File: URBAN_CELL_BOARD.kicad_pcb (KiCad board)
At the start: 2 copper layers, 162 x 181.6 mm, 18 parts, among them J1 Conn_02x09_Odd_Even, J2 Conn_01x02_Female, J3 Conn_01x02_Female

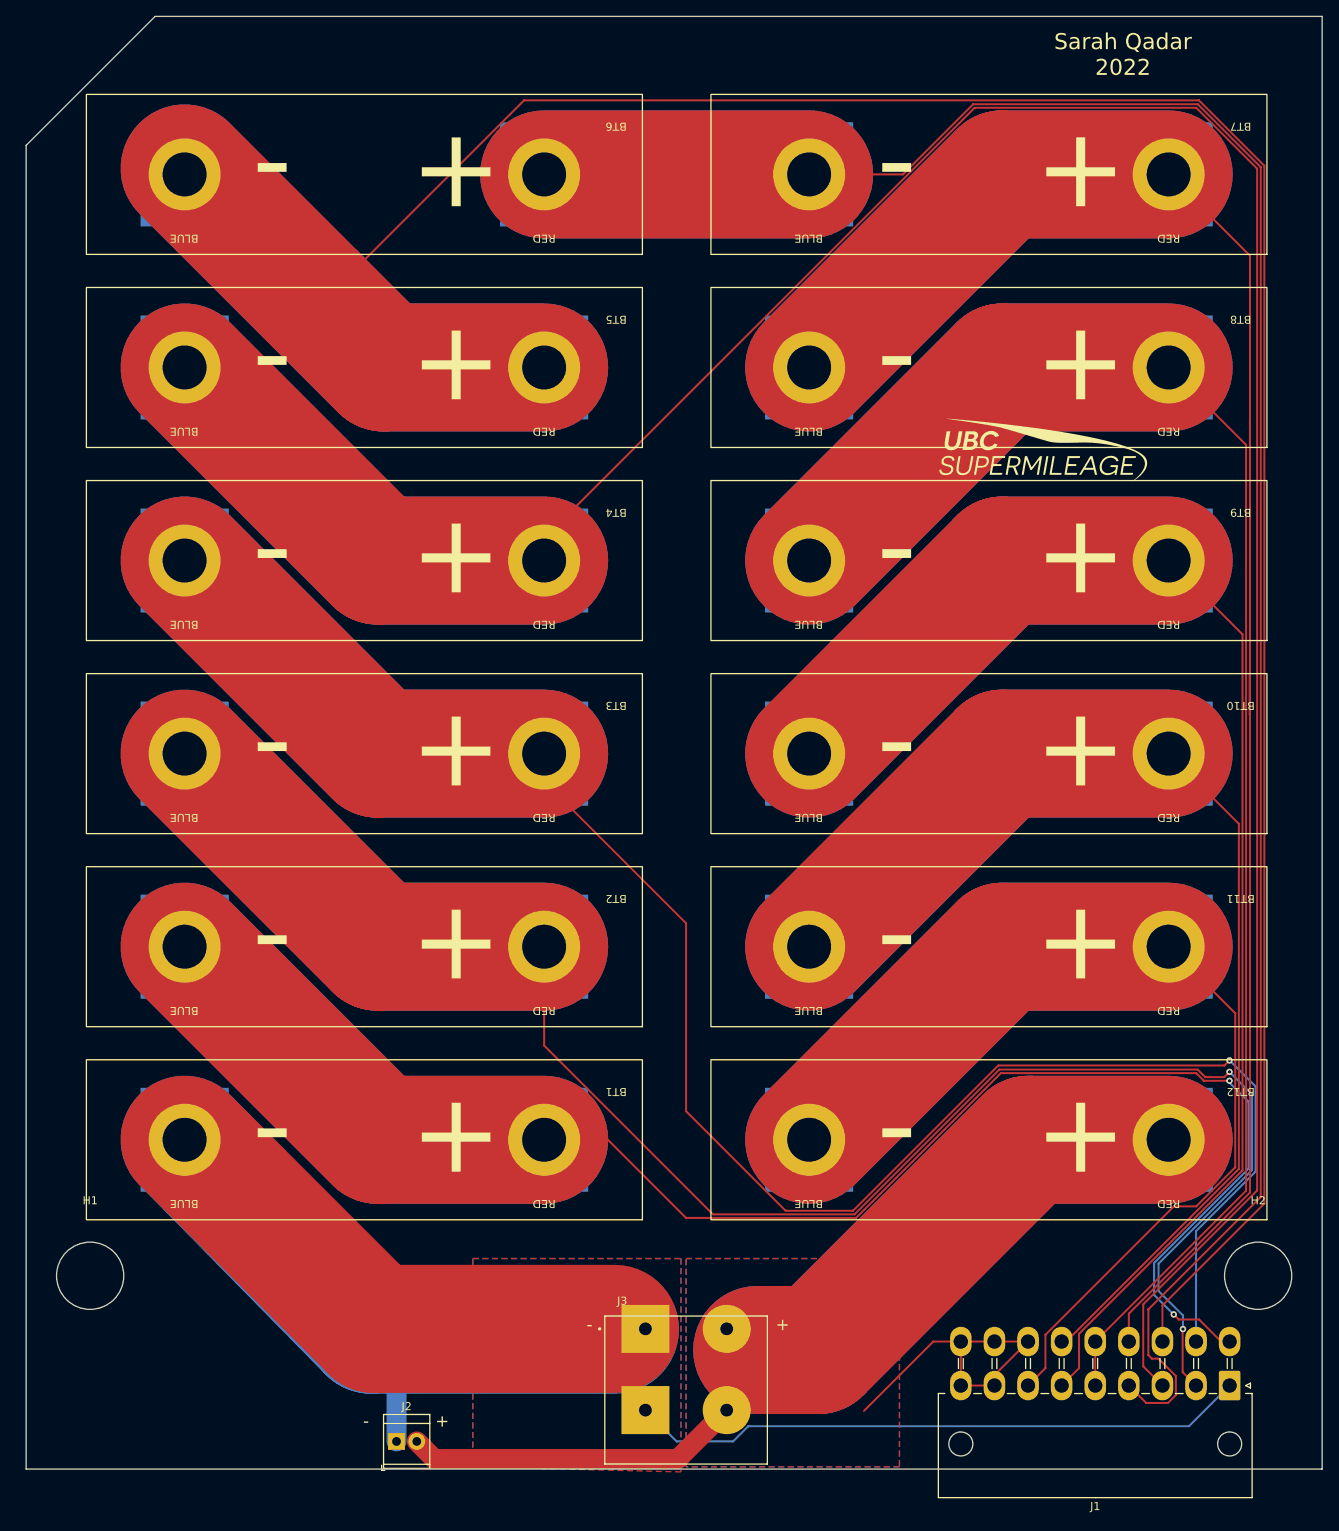
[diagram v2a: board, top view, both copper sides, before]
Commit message: fixed most layout errors/warnings
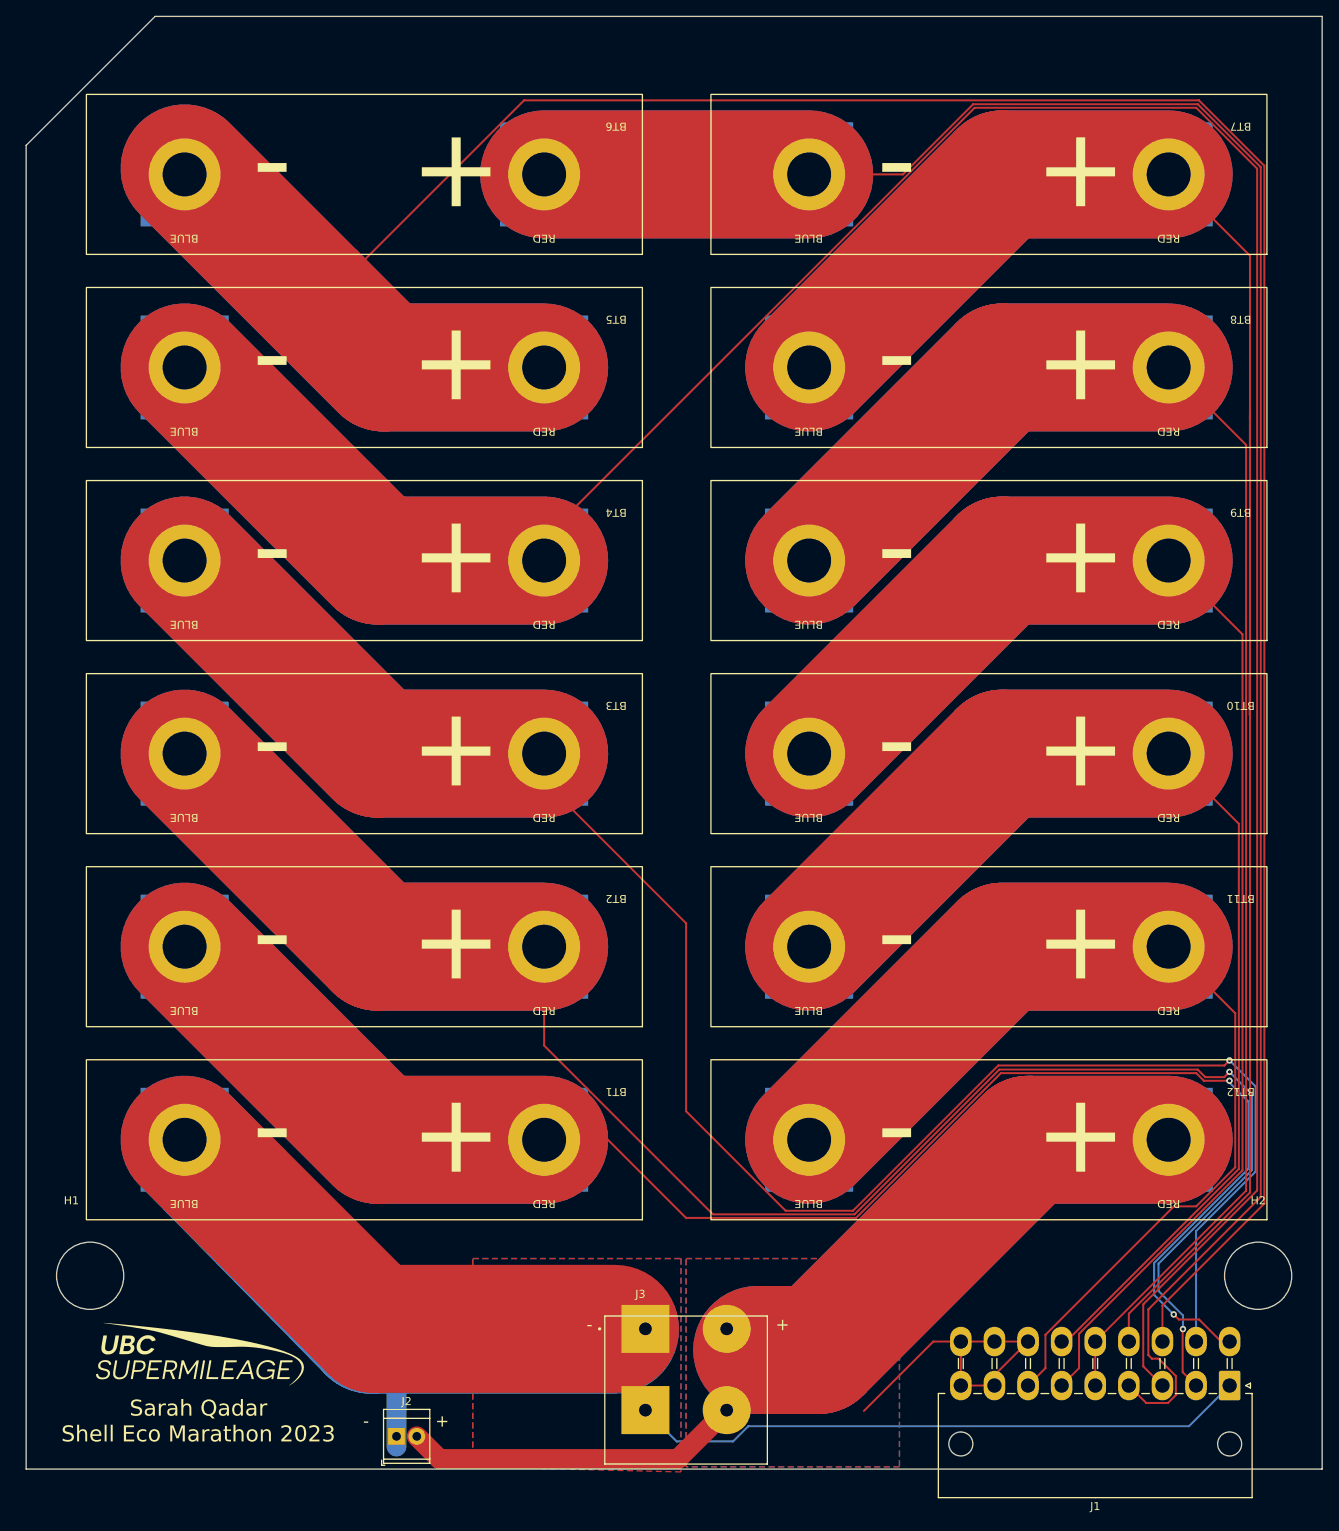
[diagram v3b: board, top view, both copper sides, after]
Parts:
- moved G*** 154.6 mm to (105.4, 268.0)
- moved J2 0.63 mm to (130.2, 277.5)
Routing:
- net cell7+: track 303.1 -> 305.0 mm
- net +48V: track 209.4 -> 208.1 mm
- net GND: track 220.2 -> 220.8 mm
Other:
- board text added: "Sarah Qadar Shell Eco Marathon 2023"
- board text removed: "Sarah Qadar 2022"
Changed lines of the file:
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@@
     (property "Sheetname" "")
     (attr through_hole)
-    (fp_text reference "J3" (at -2.905 -3.485) (layer "F.SilkS")
+    (fp_text reference "J3" (at -0.635 -4.3425) (layer "F.SilkS")
       (effects (font (size 1 1) (thickness 0.15)))
     )
@@
       (effects (font (size 1 1) (thickness 0.15)))
     )
-    (fp_text value "Conn_02x09_Odd_Even" (at 16.8 8.55) (layer "F.Fab")
+    (fp_text value "Conn_02x09_Odd_Even" (at 17.145 -7.62) (layer "F.Fab")
       (effects (font (size 1 1) (thickness 0.15)))
     )
@@
   )
   (footprint "LOGO" (layer "F.Cu")
-    (at 210.82 154.94)
+    (at 105.41 267.97)
     (attr board_only exclude_from_pos_files exclude_from_bom)
     (fp_text reference "G***" (at 0 0) (layer "F.Fab") hide
@@
   )
   (footprint "TerminalBlock_TE-Connectivity:TerminalBlock_TE_282834-2_1x02_P2.54mm_Horizontal" (layer "F.Cu")
-    (at 130.175 278.13)
+    (at 130.175 277.495)
     (descr "Terminal Block TE 282834-2, 2 pins, pitch 2.54mm, size 5.54x6.5mm^2, drill diamater 1.1mm, pad diameter 2.1mm, see http://www.te.com/commerce/DocumentDelivery/DDEController?Action=showdoc&DocId=Customer+Drawing%7F282834%7FC1%7Fpdf%7FEnglish%7FENG_CD_282834_C1.pdf, script-generated using https://github.com/pointhi/kicad-footprint-generator/scripts/TerminalBlock_TE-Connectivity")
     (tags "THT Terminal Block TE 282834-2 pitch 2.54mm size 5.54x6.5mm^2 drill 1.1mm pad 2.1mm")
@@
     (property "Sheetname" "")
     (attr exclude_from_pos_files)
-    (fp_text reference "H1" (at 0 -9.4) (layer "F.SilkS")
+    (fp_text reference "H1" (at -2.344 -9.4) (layer "F.SilkS")
       (effects (font (size 1 1) (thickness 0.15)))
     )
@@
     (effects (font (size 1.5 1.5) (thickness 0.3)) (justify mirror))
   )
-  (gr_text "Sarah Qadar\n2022" (at 220.98 104.775) (layer "F.SilkS")
+  (gr_text "Sarah Qadar\nShell Eco Marathon 2023" (at 105.41 275.59) (layer "F.SilkS")
     (effects (font (size 2 2) (thickness 0.15)))
   )
@@
   (segment (start 127 264.16) (end 157.48 264.16) (width 16) (layer "B.Cu") (net 2))
   (segment (start 234.315 271.145) (end 229.235 276.225) (width 0.25) (layer "B.Cu") (net 2))
-  (segment (start 130.175 278.13) (end 130.175 267.335) (width 2.5) (layer "B.Cu") (net 2))
   (segment (start 174.144761 276.225) (end 172.239761 278.13) (width 0.25) (layer "B.Cu") (net 2))
   (segment (start 229.235 276.225) (end 174.144761 276.225) (width 0.25) (layer "B.Cu") (net 2))
+  (segment (start 130.175 278.765) (end 130.175 267.335) (width 2.5) (layer "B.Cu") (net 2))
   (segment (start 165.2025 278.13) (end 161.29 274.2175) (width 0.25) (layer "B.Cu") (net 2))
   (segment (start 148.629 216.287) (end 127.823 216.287) (width 16) (layer "F.Cu") (net 3))
@@
   (segment (start 204.915 271.145) (end 204.915 269.845) (width 0.25) (layer "F.Cu") (net 8))
   (segment (start 200.715 271.145) (end 204.915 271.145) (width 0.25) (layer "F.Cu") (net 8))
-  (segment (start 165.3335 280.334) (end 134.919 280.334) (width 2.5) (layer "F.Cu") (net 8))
   (segment (start 200.715 265.645) (end 197.27 265.645) (width 0.25) (layer "F.Cu") (net 8))
   (segment (start 175.26 266.7) (end 182.88 266.7) (width 16) (layer "F.Cu") (net 8))
   (segment (start 200.715 265.645) (end 200.715 271.145) (width 0.25) (layer "F.Cu") (net 8))
+  (segment (start 171.45 274.2175) (end 165.3335 280.334) (width 2.5) (layer "F.Cu") (net 8))
   (segment (start 204.915 269.845) (end 209.115 265.645) (width 0.25) (layer "F.Cu") (net 8))
   (segment (start 200.715 265.645) (end 209.115 265.645) (width 0.25) (layer "F.Cu") (net 8))
-  (segment (start 171.45 274.2175) (end 165.3335 280.334) (width 2.5) (layer "F.Cu") (net 8))
+  (segment (start 165.3335 280.334) (end 135.554 280.334) (width 2.5) (layer "F.Cu") (net 8))
   (segment (start 197.27 265.645) (end 188.595 274.32) (width 0.25) (layer "F.Cu") (net 8))
   (segment (start 209.159 240.421) (end 226.695 240.421) (width 16) (layer "F.Cu") (net 8))
-  (segment (start 183.935 265.645) (end 182.88 266.7) (width 0.25) (layer "F.Cu") (net 8))
   (segment (start 182.88 266.7) (end 209.159 240.421) (width 16) (layer "F.Cu") (net 8))
-  (segment (start 134.919 280.334) (end 132.715 278.13) (width 2.5) (layer "F.Cu") (net 8))
+  (segment (start 135.554 280.334) (end 132.715 277.495) (width 2.5) (layer "F.Cu") (net 8))
   (segment (start 182.88 266.7) (end 175.26 266.7) (width 16) (layer "B.Cu") (net 8))
   (segment (start 209.159 240.421) (end 182.88 266.7) (width 16) (layer "B.Cu") (net 8))
@@
   (segment (start 226.695 216.287) (end 205.889 216.287) (width 16) (layer "B.Cu") (net 9))
   (segment (start 205.889 216.287) (end 181.755 240.421) (width 16) (layer "B.Cu") (net 9))
-  (segment (start 236.855 187.325) (end 236.855 129.91) (width 0.25) (layer "F.Cu") (net 10))
-  (segment (start 236.855 187.325) (end 236.82 187.29) (width 0.25) (layer "F.Cu") (net 10))
-  (segment (start 236.82 187.29) (end 236.82 182.245) (width 0.25) (layer "F.Cu") (net 10))
   (segment (start 236.855 182.245) (end 236.855 150.495) (width 0.25) (layer "F.Cu") (net 10))
+  (segment (start 236.855 150.495) (end 236.855 149.225) (width 0.25) (layer "F.Cu") (net 10))
+  (segment (start 236.855 149.86) (end 236.855 149.225) (width 0.25) (layer "F.Cu") (net 10))
+  (segment (start 236.855 149.225) (end 236.855 129.91) (width 0.25) (layer "F.Cu") (net 10))
+  (segment (start 236.855 129.91) (end 226.695 119.75) (width 0.25) (layer "F.Cu") (net 10))
+  (segment (start 236.855 187.325) (end 236.855 149.86) (width 0.25) (layer "F.Cu") (net 10))
   (segment (start 236.855 247.015) (end 236.855 187.325) (width 0.25) (layer "F.Cu") (net 10))
   (segment (start 221.715 262.155) (end 236.855 247.015) (width 0.25) (layer "F.Cu") (net 10))
   (segment (start 236.82 182.245) (end 236.855 182.245) (width 0.25) (layer "F.Cu") (net 10))
-  (segment (start 236.855 129.91) (end 226.695 119.75) (width 0.25) (layer "F.Cu") (net 10))
   (segment (start 226.695 119.75) (end 205.889 119.75) (width 16) (layer "F.Cu") (net 10))
+  (segment (start 236.855 187.325) (end 236.82 187.29) (width 0.25) (layer "F.Cu") (net 10))
   (segment (start 205.889 119.75) (end 181.755 143.884) (width 16) (layer "F.Cu") (net 10))
+  (segment (start 236.82 187.29) (end 236.82 182.245) (width 0.25) (layer "F.Cu") (net 10))
   (segment (start 221.715 265.645) (end 221.715 262.155) (width 0.25) (layer "F.Cu") (net 10))
+  (segment (start 236.855 150.495) (end 236.855 149.86) (width 0.25) (layer "F.Cu") (net 10))
   (segment (start 226.695 119.75) (end 205.889 119.75) (width 16) (layer "B.Cu") (net 10))
   (segment (start 205.889 119.75) (end 181.755 143.884) (width 16) (layer "B.Cu") (net 10))
